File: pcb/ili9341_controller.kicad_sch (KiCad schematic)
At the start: 133 parts, among them J1 USB_B_Micro, J2 RP_SWD_CONN, J3 CONN_RP2040, J4 CONN_FPGA, J5 CONN_TFT, J6 PWR_CONN, Q1 NPN, Q2 NPN, Q3 NPN, SW1 RP_RST_SW, SW2 RP_USB_BOOT_SW, U1 ICE40UP5K-SG48ITR, U2 LM3880, U3 TLV75512PDBV, U4 TLV75525PDBV, U5 TLV75533PDBV, U6 RP2040, U7 W25Q128JVS, Y1 12MHz

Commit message: add input buttons
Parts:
- removed J3: CONN_RP2040, symbol Connector_Generic:Conn_02x07_Counter_Clockwise
- added C34: 1u, symbol Device:C_Small
- added C35: 100n, symbol Device:C_Small
- added J3: CONN_RP2040, symbol Connector_Generic:Conn_02x05_Counter_Clockwise
- added R26, R27, R28, R29, R30, R31, R32, R33: 10k, symbol Device:R
- added SW10: SW_BUTTON_B, symbol Switch:SW_SPST
- added SW3: SW_ARROW_UP, symbol Switch:SW_SPST
- added SW4: SW_ARROW_DOWN, symbol Switch:SW_SPST
- added SW5: SW_ARROW_LEFT, symbol Switch:SW_SPST
- added SW6: SW_ARROW_RIGHT, symbol Switch:SW_SPST
- added SW7: SW_BUTTON_START, symbol Switch:SW_SPST
- added SW8: SW_BUTTON_SEL, symbol Switch:SW_SPST
- added SW9: SW_BUTTON_A, symbol Switch:SW_SPST
- added TP46, TP47, TP48, TP49, TP50, TP51, TP52, TP53, TP54, TP55, TP56, TP57: TestPoint, symbol Connector:TestPoint
- added U9: 74LS151, symbol 74xx:74LS151
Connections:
- net +3V3: now also C34.1, C35.1, SW10.1 (A), SW3.1 (A), SW4.1 (A), SW5.1 (A), SW6.1 (A), SW7.1 (A), SW8.1 (A), SW9.1 (A), U9.16 (VCC)
- net GND: now also C34.2, C35.2, R26.2, R27.2, R28.2, R29.2, R30.2, R31.2, R32.2, R33.2, U9.7 (~{E}), U9.8 (GND)
- net RP2040_GPIO17: now also J3.1 (Pin_1)
- net RP2040_GPIO18: now also J3.2 (Pin_2)
- net RP2040_GPIO19: now also J3.3 (Pin_3)
- net RP2040_GPIO20: now also J3.4 (Pin_4)
- net RP2040_GPIO21: now also J3.5 (Pin_5)
- net RP2040_GPIO22: now also J3.6 (Pin_6)
- net RP2040_GPIO26: now also J3.7 (Pin_7)
- net RP2040_GPIO27: now also J3.8 (Pin_8)
- net RP2040_GPIO28: now also J3.9 (Pin_9)
- net RP2040_GPIO29: now also J3.10 (Pin_10)
- net RP2040_GPIO13 renamed BTN_MUX_S0
- net BTN_MUX_S0: now also TP54.1, U9.11 (S0)
- net RP2040_GPIO14 renamed BTN_MUX_S1
- net BTN_MUX_S1: now also TP55.1, U9.10 (S1)
- net RP2040_GPIO15 renamed BTN_MUX_S2
- net BTN_MUX_S2: now also TP56.1, U9.9 (S2)
- net RP2040_GPIO16 renamed BTN_MUX_OUT
- net BTN_MUX_OUT: now also TP57.1, U9.5 (Z)
- new net ARROW_DOWN: R32.1, SW4.2 (B), TP52.1, U9.3 (I1)
- new net ARROW_LEFT: R31.1, SW5.2 (B), TP51.1, U9.2 (I2)
- new net ARROW_RIGHT: R30.1, SW6.2 (B), TP50.1, U9.1 (I3)
- new net ARROW_UP: R33.1, SW3.2 (B), TP53.1, U9.4 (I0)
- new net BUTTON_A: R27.1, SW9.2 (B), TP47.1, U9.13 (I6)
- new net BUTTON_B: R26.1, SW10.2 (B), TP46.1, U9.12 (I7)
- new net BUTTON_SEL: R28.1, SW8.2 (B), TP48.1, U9.14 (I5)
- new net BUTTON_START: R29.1, SW7.2 (B), TP49.1, U9.15 (I4)
- no-connect marks 2 -> 3
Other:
- note added: "Input Buttons & Multiplexer & Decoupling Capacitors"
- note added: "Note: 74HC151 may be used for greater power efficiency."
- moved on the sheet: D10, D7, D8, D9, J4, J5, Q1, Q2, Q3, R19, R20, R21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

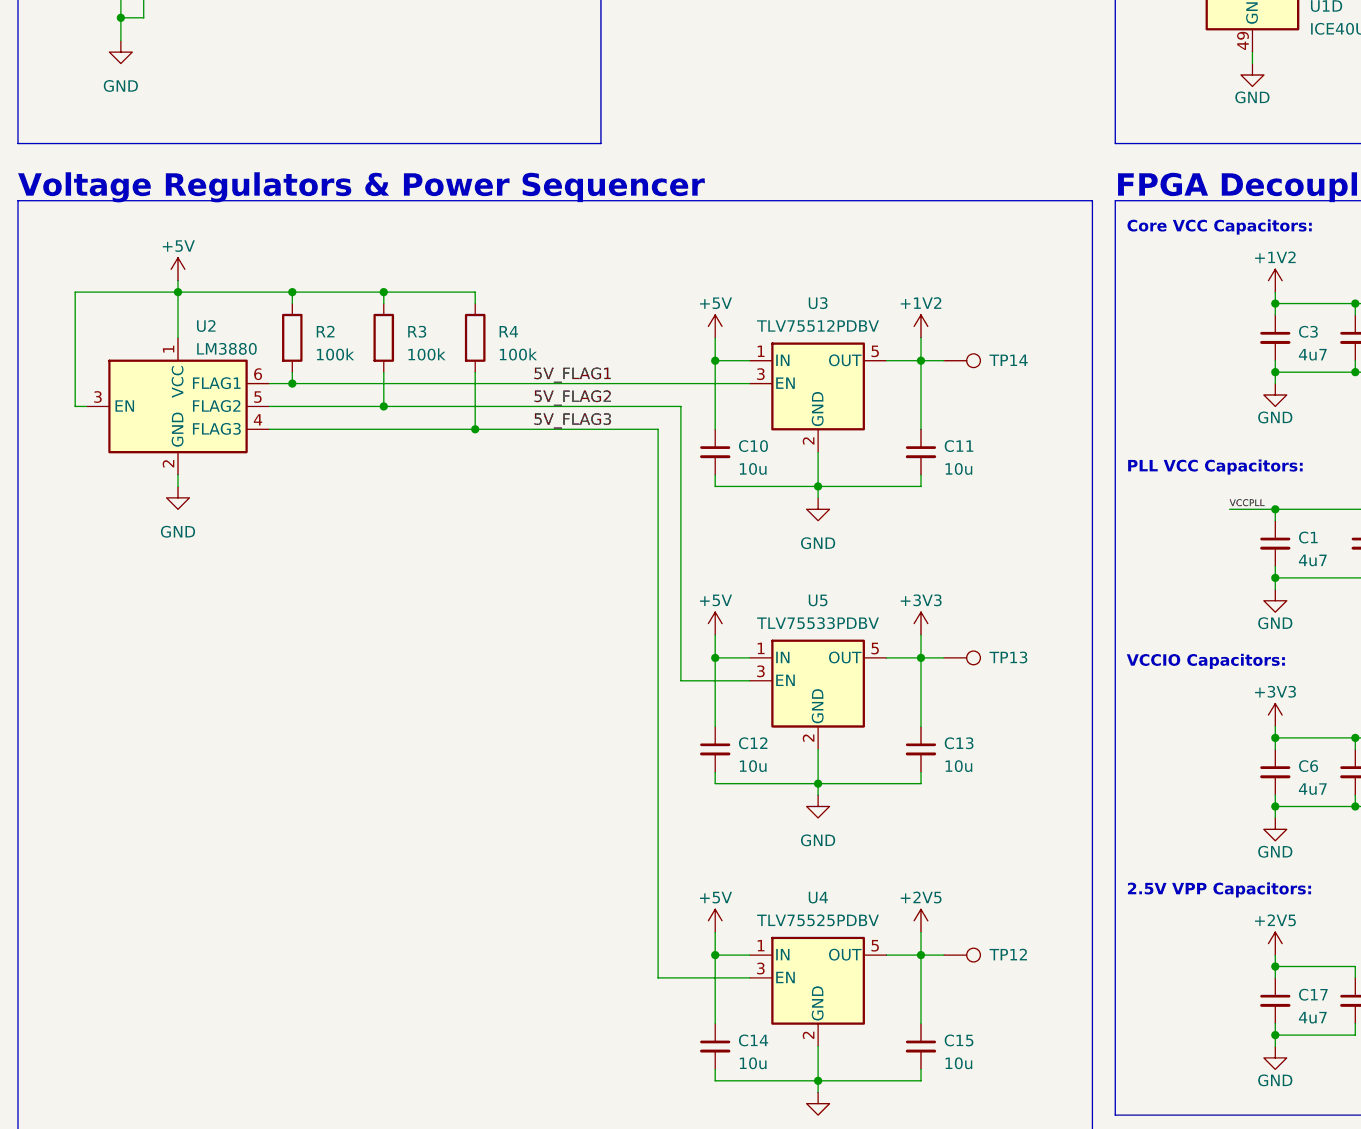
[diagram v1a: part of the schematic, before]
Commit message: add power jumper headers
for current measurement & voltage verification
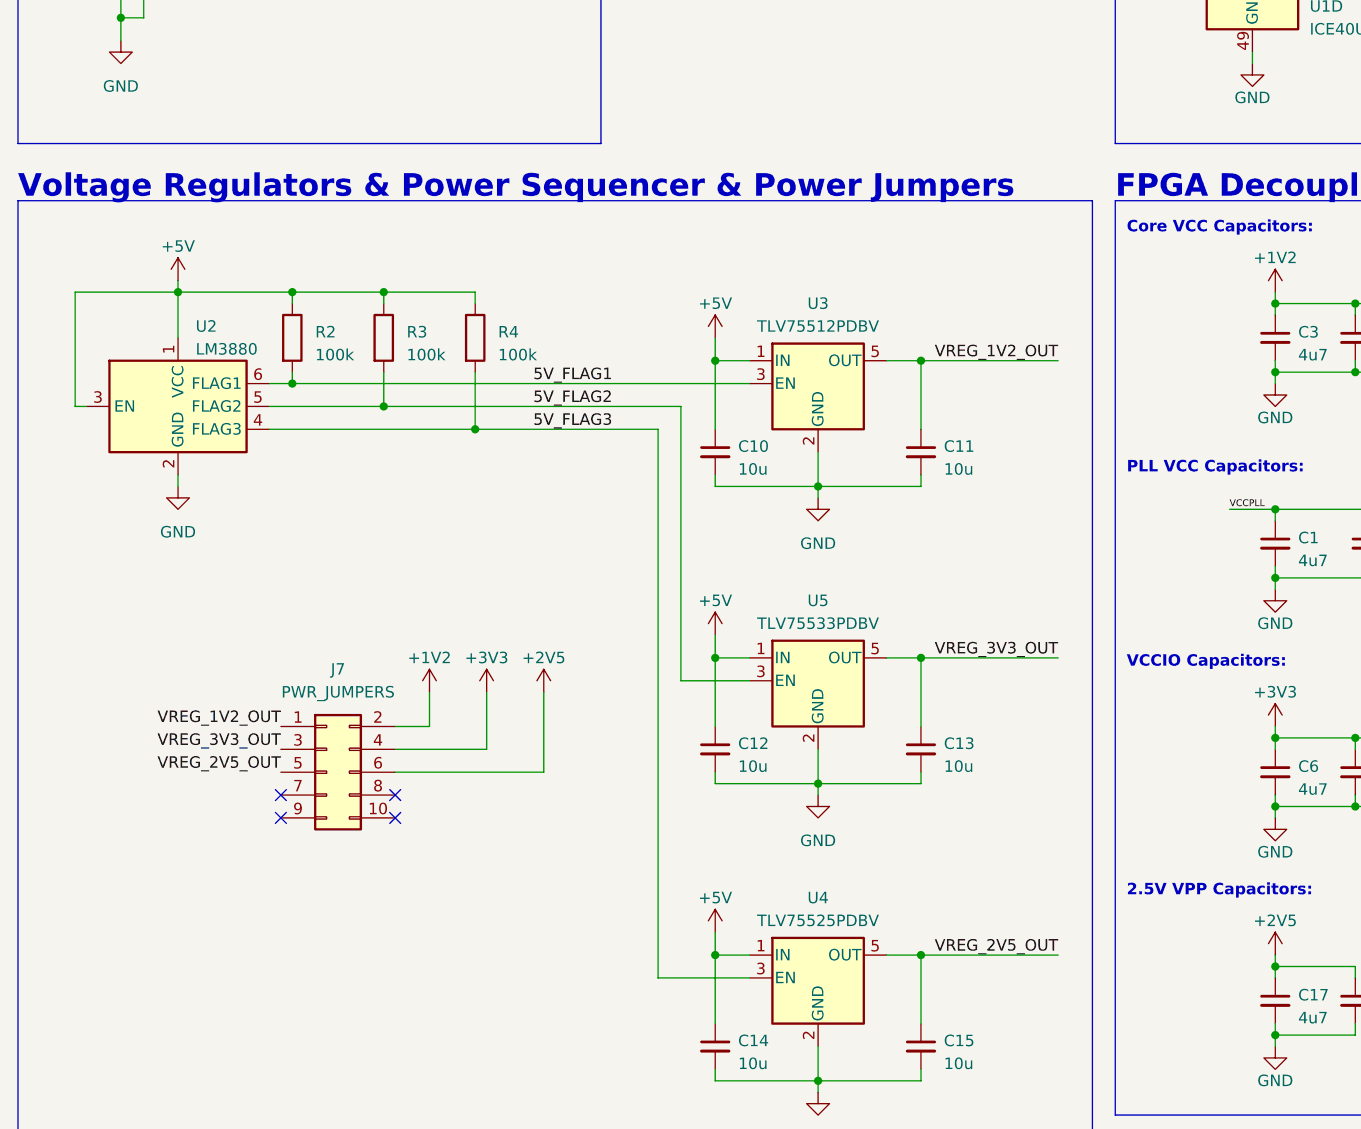
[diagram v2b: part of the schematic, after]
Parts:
- removed TP12, TP13, TP14: TestPoint, symbol Connector:TestPoint
- added J7: PWR_JUMPERS, symbol Connector_Generic:Conn_02x05_Odd_Even
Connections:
- net +1V2: now also J7.2 (Pin_2); no longer C11.1, U3.5 (OUT)
- net +2V5: now also J7.6 (Pin_6); no longer C15.1, U4.5 (OUT)
- net +3V3: now also J7.4 (Pin_4); no longer C13.1, U5.5 (OUT)
- new net VREG_1V2_OUT: C11.1, J7.1 (Pin_1), U3.5 (OUT)
- new net VREG_2V5_OUT: C15.1, J7.5 (Pin_5), U4.5 (OUT)
- new net VREG_3V3_OUT: C13.1, J7.3 (Pin_3), U5.5 (OUT)
- no-connect marks 3 -> 7
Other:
- note added: "Voltage Regulators & Power Sequencer & Power Jumpers"
- note removed: "Voltage Regulators & Power Sequencer"

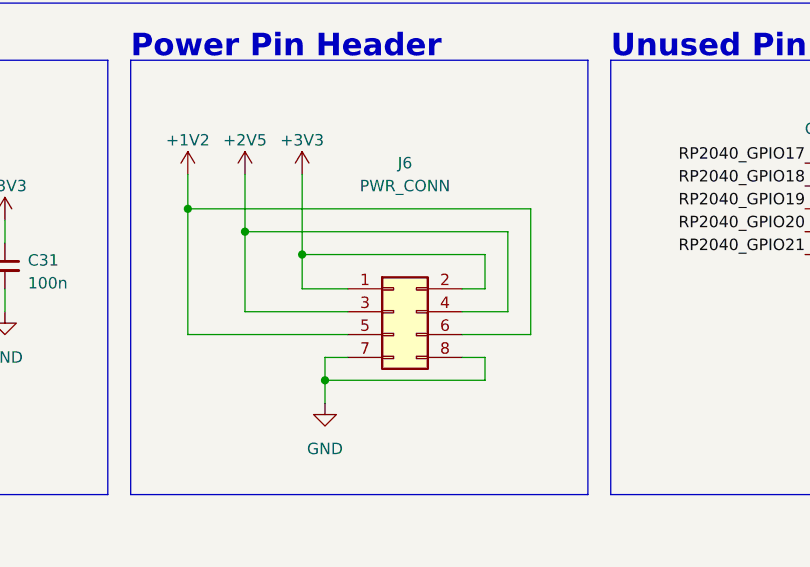
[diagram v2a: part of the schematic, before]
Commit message: replace power connector with 02x05 instead of 02x04
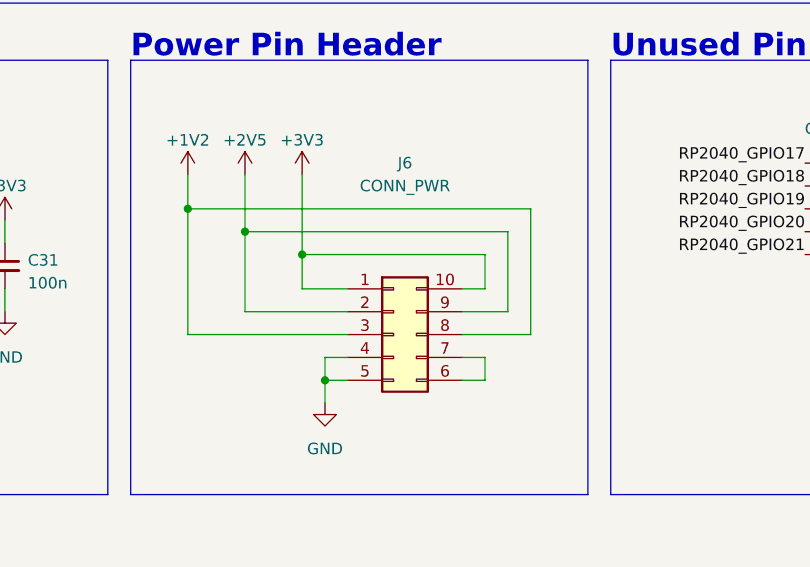
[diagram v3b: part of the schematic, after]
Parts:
- removed J6: PWR_CONN, symbol Connector_Generic:Conn_02x04_Odd_Even
- added J6: CONN_PWR, symbol Connector_Generic:Conn_02x05_Counter_Clockwise
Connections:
- net +1V2: now also J6.3 (Pin_3), J6.8 (Pin_8)
- net +2V5: now also J6.2 (Pin_2), J6.9 (Pin_9)
- net +3V3: now also J6.1 (Pin_1), J6.10 (Pin_10)
- net GND: now also J6.4 (Pin_4), J6.5 (Pin_5)
- new net: J6.6 (Pin_6), J6.7 (Pin_7)
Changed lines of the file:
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@@
   (junction (at 528.32 320.04) (diameter 0) (color 0 0 0 0)
   )
-  (junction (at 146.05 360.68) (diameter 0) (color 0 0 0 0)
-  )
   (junction (at 401.32 393.7) (diameter 0) (color 0 0 0 0)
   )
@@
   (junction (at 384.81 43.18) (diameter 0) (color 0 0 0 0)
   )
+  (junction (at 146.05 360.68) (diameter 0) (color 0 0 0 0)
+  )
   (junction (at 334.01 200.66) (diameter 0) (color 0 0 0 0)
   )
@@
     (stroke (width 0) (type default))
   )
-  (wire (pts (xy 146.05 360.68) (xy 163.83 360.68))
-    (stroke (width 0) (type default))
-  )
   (wire (pts (xy 114.3 144.78) (xy 114.3 146.05))
     (stroke (width 0) (type default))
@@
     (stroke (width 0) (type default))
   )
+  (wire (pts (xy 146.05 360.68) (xy 146.05 363.22))
+    (stroke (width 0) (type default))
+  )
   (wire (pts (xy 358.14 171.45) (xy 365.76 171.45))
     (stroke (width 0) (type default))
@@
     (stroke (width 0) (type default))
   )
+  (wire (pts (xy 146.05 360.68) (xy 148.59 360.68))
+    (stroke (width 0) (type default))
+  )
   (wire (pts (xy 166.37 344.17) (xy 166.37 353.06))
     (stroke (width 0) (type default))
@@
     (stroke (width 0) (type default))
   )
+  (wire (pts (xy 161.29 360.68) (xy 163.83 360.68))
+    (stroke (width 0) (type default))
+  )
   (wire (pts (xy 138.43 237.49) (xy 156.21 237.49))
     (stroke (width 0) (type default))
@@
     (stroke (width 0) (type default))
   )
-  (wire (pts (xy 146.05 358.14) (xy 146.05 360.68))
-    (stroke (width 0) (type default))
-  )
   (wire (pts (xy 434.34 289.56) (xy 434.34 303.53))
     (stroke (width 0) (type default))
@@
     (stroke (width 0) (type default))
   )
-  (wire (pts (xy 146.05 360.68) (xy 146.05 363.22))
+  (wire (pts (xy 146.05 358.14) (xy 146.05 360.68))
     (stroke (width 0) (type default))
   )
@@
     )
   )
-  (symbol (lib_id "Connector_Generic:Conn_02x04_Odd_Even") (at 153.67 353.06 0) (unit 1)
+  (symbol (lib_id "Connector_Generic:Conn_02x05_Counter_Clockwise") (at 153.67 355.6 0) (unit 1)
     (in_bom yes) (on_board yes) (dnp no)
     (property "Reference" "J6" (at 154.94 336.55 0)
       (effects (font (size 1.27 1.27)))
     )
-    (property "Value" "PWR_CONN" (at 154.94 339.09 0)
+    (property "Value" "CONN_PWR" (at 154.94 339.09 0)
       (effects (font (size 1.27 1.27)))
     )
-    (property "Footprint" "" (at 153.67 353.06 0)
+    (property "Footprint" "" (at 153.67 355.6 0)
       (effects (font (size 1.27 1.27)) hide)
     )
-    (property "Datasheet" "~" (at 153.67 353.06 0)
+    (property "Datasheet" "~" (at 153.67 355.6 0)
       (effects (font (size 1.27 1.27)) hide)
     )
     (pin "1")
+    (pin "10")
     (pin "2")
     (pin "3")
@@
     (pin "7")
     (pin "8")
+    (pin "9")
     (instances
       (project "ili9341_controller"
